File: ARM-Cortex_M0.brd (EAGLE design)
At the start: 50 x 50 mm, 26 parts, among them IC1 SAMD21G18A-AUT, J2 CORTEX_DEBUGPTH, U1 MIC5203-3.3, X1 MINI-USB_SHIELD4P-32005-101, Y3 32,768Khz_SMD

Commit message: hardware modifications
hardware modifications
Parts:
- removed J11: (no value), SparkFun-Connectors:USB-B-MICRO-SMD_V03
- removed X1: MINI-USB_SHIELD4P-32005-101, con-cypressindustries:32005-101
- added J13: USB-MICROB", KarlVaello-Connectors:USB-B-MICRO-SMD_V03
- moved C8 5.00 mm to (16.4, 12.6)
- moved R1 1.14 mm to (19.1, 12.6)
- moved R2 0.30 mm to (19.1, 16.6)
- moved C4 0.30 mm to (24.3, 16.6)
- moved C5 0.22 mm to (21.7, 16.6)
- moved C6 0.10 mm to (24.8, 33.1)
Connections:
- net GND: now also J13.GND, J13.SHIELD1, J13.SHIELD2, J13.SHIELD3; no longer J11.GND, J11.SHIELD1, J11.SHIELD2, J11.SHIELD3
- net TARGET_USB_N: now also J13.D-; no longer J11.D-
- net TARGET_USB_P: now also J13.D+; no longer J11.D+
- net VBUS: now also J13.VBUS; no longer J11.VBUS
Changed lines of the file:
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@@
 <layer number="23" name="tOrigins" color="15" fill="1" visible="yes" active="yes"/>
 <layer number="24" name="bOrigins" color="15" fill="1" visible="yes" active="yes"/>
-<layer number="25" name="tNames" color="7" fill="1" visible="yes" active="yes"/>
-<layer number="26" name="bNames" color="7" fill="1" visible="yes" active="yes"/>
-<layer number="27" name="tValues" color="7" fill="1" visible="yes" active="yes"/>
-<layer number="28" name="bValues" color="7" fill="1" visible="yes" active="yes"/>
+<layer number="25" name="tNames" color="7" fill="1" visible="no" active="yes"/>
+<layer number="26" name="bNames" color="7" fill="1" visible="no" active="yes"/>
+<layer number="27" name="tValues" color="7" fill="1" visible="no" active="yes"/>
+<layer number="28" name="bValues" color="7" fill="1" visible="no" active="yes"/>
 <layer number="29" name="tStop" color="7" fill="3" visible="no" active="yes"/>
 <layer number="30" name="bStop" color="7" fill="6" visible="no" active="yes"/>
@@
 <element name="C2" library="KarlVaello-Capacitors" package="C0603" value="22pF" x="14" y="29.5" rot="R90"/>
 <element name="C3" library="KarlVaello-Capacitors" package="C0603" value="100nF" x="33.1" y="28.6" rot="R180"/>
-<element name="C4" library="KarlVaello-Capacitors" package="C0603" value="" x="24.3" y="16.9" rot="R270"/>
-<element name="C5" library="KarlVaello-Capacitors" package="C0603" value="100nF" x="21.5" y="16.5" rot="R90"/>
+<element name="C4" library="KarlVaello-Capacitors" package="C0603" value="" x="24.3" y="16.6" rot="R270"/>
+<element name="C5" library="KarlVaello-Capacitors" package="C0603" value="100nF" x="21.7" y="16.6" rot="R90"/>
 <element name="J2" library="SparkFun-Connectors" package="2X5-PTH-1.27MM" value="CORTEX_DEBUGPTH" x="8.5" y="27.1" rot="R90"/>
-<element name="C6" library="KarlVaello-Capacitors" package="C0603" value="1uF" x="24.7" y="33.1" rot="R270"/>
+<element name="C6" library="KarlVaello-Capacitors" package="C0603" value="1uF" x="24.8" y="33.1" rot="R270"/>
 <element name="U1" library="SparkFun-PowerIC" package="SOT23-5" value="MIC5203-3.3" x="12.9" y="17">
 <attribute name="PROD_ID" value="VREG-00822" x="12.9" y="17" size="1.778" layer="27" display="off"/>
@@
 <element name="J9" library="SparkFun-Connectors" package="1X01NS-KIT" value="" x="2.9" y="6.1"/>
 <element name="J10" library="SparkFun-Connectors" package="1X01NS-KIT" value="" x="2.9" y="4"/>
-<element name="J11" library="SparkFun-Connectors" package="USB-B-MICRO-SMD_V03" value="" x="48" y="25" rot="R180">
-<attribute name="PROD_ID" value="CONN-11752" x="48" y="25" size="1.778" layer="27" rot="R180" display="off"/>
-</element>
-<element name="X1" library="con-cypressindustries" package="32005-101" value="MINI-USB_SHIELD4P-32005-101" x="46.5" y="13.9" rot="R180">
-<attribute name="OC_NEWARK" value="unknown" x="46.5" y="13.9" size="1.778" layer="27" rot="R180" display="off"/>
-<attribute name="OC_FARNELL" value="unknown" x="46.5" y="13.9" size="1.778" layer="27" rot="R180" display="off"/>
-<attribute name="MPN" value="" x="46.5" y="13.9" size="1.778" layer="27" rot="R180" display="off"/>
-<attribute name="MF" value="" x="46.5" y="13.9" size="1.778" layer="27" rot="R180" display="off"/>
-</element>
 <element name="S1" library="SparkFun-Electromechanical" package="TACTILE-SWITCH-SMD" value="SW-MOME" x="42.8" y="4.1">
 <attribute name="PROD_ID" value="SWCH-08247" x="42.8" y="4.1" size="1.778" layer="27" display="off"/>
 </element>
-<element name="C8" library="KarlVaello-Capacitors" package="C0603" value="10nF" x="21.3" y="11.6" rot="R270"/>
-<element name="R1" library="KarlVaello-Resistors" package="R0603" value="330R" x="18.2" y="11.9" rot="R90"/>
-<element name="R2" library="KarlVaello-Resistors" package="R0603" value="10K" x="18.8" y="16.6" rot="R90"/>
+<element name="C8" library="KarlVaello-Capacitors" package="C0603" value="10nF" x="16.4" y="12.6" rot="R270"/>
+<element name="R1" library="KarlVaello-Resistors" package="R0603" value="330R" x="19.1" y="12.6" rot="R90"/>
+<element name="R2" library="KarlVaello-Resistors" package="R0603" value="10K" x="19.1" y="16.6" rot="R90"/>
+<element name="J13" library="KarlVaello-Connectors" package="USB-B-MICRO-SMD_V03" value="USB-MICROB&quot;" x="48" y="25" rot="R180">
+<attribute name="PROD_ID" value="CONN-11752" x="48" y="25" size="1.778" layer="27" rot="R180" display="off"/>
+</element>
 </elements>
 <signals>
@@
 </polygon>
 <via x="3" y="47" extent="1-16" drill="0.6" shape="square"/>
-<wire x1="20.725" y1="25.75" x2="19" y2="25.75" width="0.3" layer="1"/>
-<wire x1="19" y1="25.75" x2="19" y2="26" width="0.3" layer="1"/>
+<wire x1="20.725" y1="25.75" x2="19" y2="25.75" width="0.2" layer="1"/>
 <contactref element="IC1" pad="18"/>
 <contactref element="C3" pad="1"/>
 <contactref element="IC1" pad="35"/>
 <contactref element="C4" pad="2"/>
-<wire x1="29.275" y1="27.25" x2="27.5" y2="27.25" width="0.3" layer="1"/>
-<wire x1="27.5" y1="27.25" x2="27.5" y2="27" width="0.3" layer="1"/>
+<wire x1="29.275" y1="27.25" x2="27.5" y2="27.25" width="0.2" layer="1"/>
 <wire x1="24.75" y1="20.725" x2="24.75" y2="22.55" width="0.3" layer="1"/>
 <wire x1="24.75" y1="22.55" x2="24.8" y2="22.6" width="0.3" layer="1"/>
@@
 <contactref element="U1" pad="2"/>
 <contactref element="C7" pad="1"/>
-<contactref element="J11" pad="GND"/>
-<contactref element="J11" pad="SHIELD1"/>
-<contactref element="J11" pad="SHIELD3"/>
-<contactref element="J11" pad="SHIELD2"/>
 <contactref element="S1" pad="3"/>
 <contactref element="C8" pad="1"/>
-<wire x1="27.5" y1="27.25" x2="25.25" y2="29.275" width="0" layer="19" extent="1-1"/>
+<contactref element="J13" pad="GND"/>
+<contactref element="J13" pad="SHIELD2"/>
+<contactref element="J13" pad="SHIELD1"/>
+<contactref element="J13" pad="SHIELD3"/>
+<wire x1="25.25" y1="29.275" x2="25.2" y2="29.275" width="0.1524" layer="1"/>
+<wire x1="25.2" y1="29.275" x2="25.2" y2="30.2" width="0.1524" layer="1"/>
 </signal>
 <signal name="+3V3">
@@
 <wire x1="24.25" y1="29.275" x2="29.275" y2="27.75" width="0" layer="19" extent="1-1"/>
 <wire x1="24.25" y1="20.725" x2="24.25" y2="29.275" width="0" layer="19" extent="1-1"/>
-<wire x1="24.3" y1="17.75" x2="24.25" y2="20.725" width="0" layer="19" extent="1-1"/>
-<wire x1="21.5" y1="17.35" x2="24.3" y2="17.75" width="0" layer="19" extent="1-1"/>
-<wire x1="18.8" y1="17.45" x2="21.5" y2="17.35" width="0" layer="19" extent="1-1"/>
-<wire x1="11.95" y1="18.3001" x2="18.8" y2="17.45" width="0" layer="19" extent="1-1"/>
+<wire x1="24.3" y1="17.45" x2="24.25" y2="20.725" width="0" layer="19" extent="1-1"/>
+<wire x1="21.7" y1="17.45" x2="24.3" y2="17.45" width="0" layer="19" extent="1-1"/>
+<wire x1="19.1" y1="17.45" x2="21.7" y2="17.45" width="0" layer="19" extent="1-1"/>
+<wire x1="11.95" y1="18.3001" x2="19.1" y2="17.45" width="0" layer="19" extent="1-1"/>
 <wire x1="9.15" y1="22.5" x2="11.95" y2="18.3001" width="0" layer="19" extent="1-1"/>
 <wire x1="9.135" y1="24.56" x2="9.15" y2="22.5" width="0" layer="19" extent="1-1"/>
@@
 <contactref element="R2" pad="1"/>
 <contactref element="S1" pad="1"/>
-<wire x1="18.2" y1="12.75" x2="40.006" y2="6.005" width="0" layer="19" extent="1-1"/>
-<wire x1="18.8" y1="15.75" x2="18.2" y2="12.75" width="0" layer="19" extent="1-1"/>
-<wire x1="7.865" y1="29.64" x2="18.8" y2="15.75" width="0" layer="19" extent="1-1"/>
+<wire x1="19.1" y1="13.45" x2="40.006" y2="6.005" width="0" layer="19" extent="1-1"/>
+<wire x1="19.1" y1="15.75" x2="19.1" y2="13.45" width="0" layer="19" extent="1-1"/>
+<wire x1="7.865" y1="29.64" x2="19.1" y2="15.75" width="0" layer="19" extent="1-1"/>
 </signal>
 <signal name="N$7">
 <contactref element="IC1" pad="43"/>
 <contactref element="C6" pad="2"/>
-<wire x1="24.75" y1="29.275" x2="24.7" y2="32.25" width="0" layer="19" extent="1-1"/>
+<wire x1="24.75" y1="29.275" x2="24.8" y2="32.25" width="0" layer="19" extent="1-1"/>
 </signal>
 <signal name="RAW">
@@
 <wire x1="11.95" y1="15.6999" x2="13.85" y2="15.6999" width="0" layer="19" extent="1-1"/>
 </signal>
-<signal name="VBUS">
-<contactref element="J11" pad="VBUS"/>
-</signal>
 <signal name="TARGET_USB_N">
-<contactref element="J11" pad="D-"/>
 <contactref element="IC1" pad="33"/>
 <wire x1="29.275" y1="26.25" x2="40.25" y2="26.25" width="0.1524" layer="1"/>
 <wire x1="40.25" y1="26.25" x2="42.15" y2="24.35" width="0.1524" layer="1"/>
+<contactref element="J13" pad="D-"/>
 <wire x1="42.15" y1="24.35" x2="45.275" y2="24.35" width="0.1524" layer="1"/>
 </signal>
 <signal name="TARGET_USB_P">
-<contactref element="J11" pad="D+"/>
 <contactref element="IC1" pad="34"/>
 <wire x1="29.275" y1="26.75" x2="40.55" y2="26.75" width="0.1524" layer="1"/>
 <wire x1="40.55" y1="26.75" x2="42.3" y2="25" width="0.1524" layer="1"/>
+<contactref element="J13" pad="D+"/>
 <wire x1="42.3" y1="25" x2="45.275" y2="25" width="0.1524" layer="1"/>
 </signal>
@@
 <contactref element="C8" pad="2"/>
 <contactref element="R1" pad="1"/>
-<wire x1="21.3" y1="10.75" x2="26.25" y2="29.275" width="0" layer="19" extent="1-1"/>
-<wire x1="18.2" y1="11.05" x2="21.3" y2="10.75" width="0" layer="19" extent="1-1"/>
+<wire x1="19.1" y1="11.75" x2="26.25" y2="29.275" width="0" layer="19" extent="1-1"/>
+<wire x1="16.4" y1="11.75" x2="19.1" y2="11.75" width="0" layer="19" extent="1-1"/>
 </signal>
 <signal name="D13">
@@
 <contactref element="IC1" pad="16"/>
 </signal>
+<signal name="VBUS">
+<contactref element="J13" pad="VBUS"/>
+</signal>
 </signals>

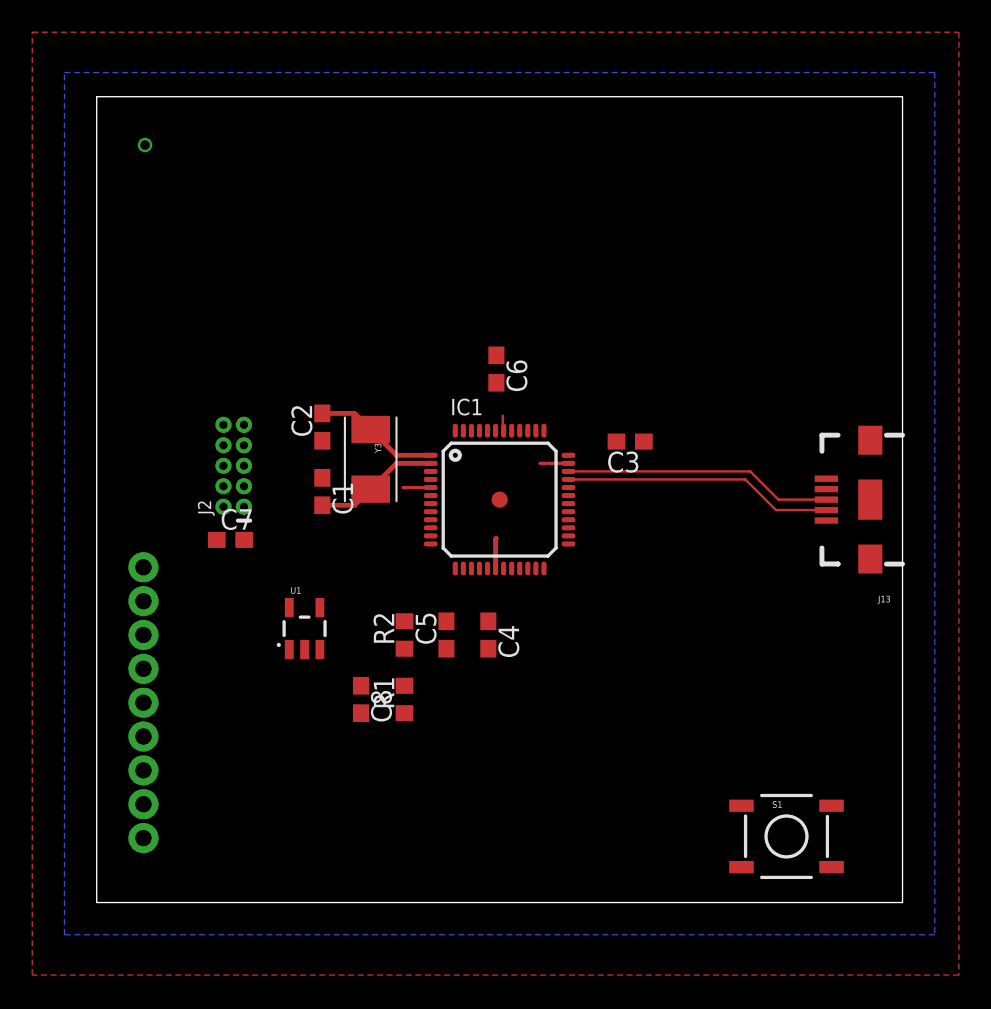
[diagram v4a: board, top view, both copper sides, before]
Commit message: Hardaware modification, programing ARM info
Hardaware modification, programing ARM info
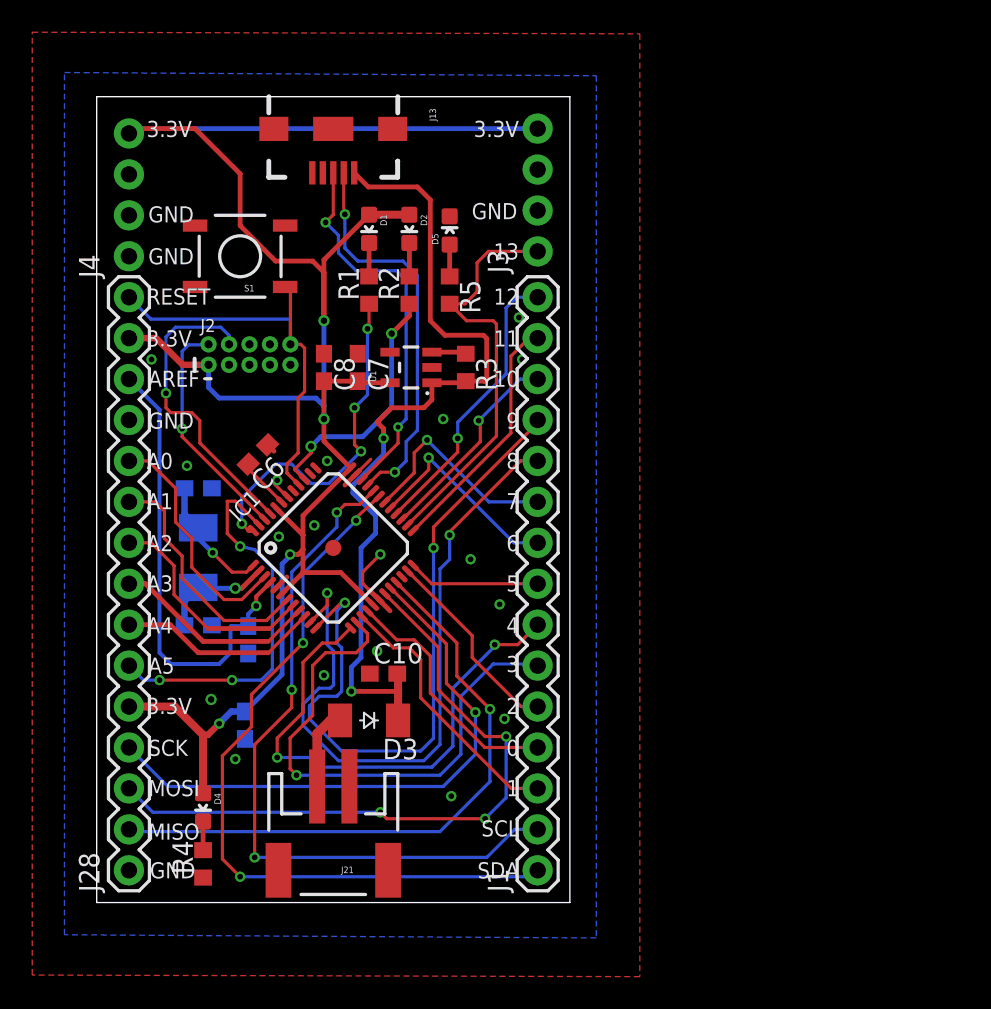
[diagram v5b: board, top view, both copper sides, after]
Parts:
- removed C3: 100nF, KarlVaello-Capacitors:C0603
- removed C4: (no value), KarlVaello-Capacitors:C0603
- removed J10, J5, J6, J7, J8, J9: (no value), SparkFun-Connectors:1X01NS-KIT
- added C10: 10uF, KarlVaello-Capacitors:C0603
- added C9: 1uF, KarlVaello-Capacitors:C0603
- added D1, D5: GREEN, SparkFun-LED:LED-0603
- added D2: YELLOW, SparkFun-LED:LED-0603
- added D3: MBR120, diode:SOD-123_MINI-SMA
- added D4: ORANGE, SparkFun-LED:LED-0603
- added J21: (no value), SparkFun-Connectors:JST-2-SMD
- added J28: (no value), SparkFun-Connectors:1X15
- added R3: 100K, KarlVaello-Resistors:R0603
- added R4, R5: 1K, KarlVaello-Resistors:R0603
- C5: value 100nF -> 10uF
- C8: value 10nF -> 10uF
- J1: device SparkFun-Connectors:1X01NS-KIT -> SparkFun-Connectors:1X15
- J3, J4: device SparkFun-Connectors:1X01NS-KIT -> SparkFun-Connectors:1X04_NO_SILK_ALL_ROUND
- R1: value 330R -> 1K
- R2: value 10K -> 1K
- U1: value MIC5203-3.3 -> SPX3918-3.3
- moved S1 49.4 mm to (8.90, 40.1), turned to 180 degrees
- moved J13 40.5 mm to (14.7, 48.0), turned to 270 degrees
- moved J3 32.7 mm to (27.4, 40.4), turned to 90 degrees
- moved J1 30.9 mm to (27.4, 2.00), turned to 90 degrees
- moved R1 25.5 mm to (16.9, 38.0)
- moved J4 23.5 mm to (2.00, 40.1), turned to 90 degrees
- moved R2 21.4 mm to (19.4, 38.0)
- moved C8 20.7 mm to (14.1, 33.2)
- moved U1 17.5 mm to (19.5, 33.2), turned to 90 degrees
- moved C6 15.7 mm to (10.0, 27.8), turned to 225 degrees
- moved C5 13.7 mm to (9.20, 11.0), flipped to the bottom
- moved C7 13.3 mm to (16.2, 33.2), turned to 270 degrees
- moved Y3 12.3 mm to (6.30, 21.4), flipped to the bottom
- moved C1 11.3 mm to (6.30, 17.2), flipped to the bottom, turned to 0 degrees
- moved IC1 10.7 mm to (14.7, 22.0), turned to 45 degrees
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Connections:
- removed net D0: IC1.16
- removed net D1: IC1.15
- removed net RAW: U1.1, U1.3
- removed net TARGE_RESET: C8.2, IC1.40, R1.1
- removed net VDDANA: IC1.6
- new net A0: IC1.3, J28.11
- new net A1: IC1.7, J28.10
- new net A2: IC1.8, J28.9
- new net A3: IC1.9, J28.8
- new net A4: IC1.10, J28.7
- new net A5: IC1.47, J28.6
- new net AREF: C9.2, IC1.4, J28.13
- new net D0/RX: IC1.16, J1.4
- new net D1/TX: IC1.15, J1.3
- new net MISO: IC1.21, J28.2
- new net MOSI: IC1.19, J28.3
- new net N$10: D5.A, R5.1
- new net N$3: IC1.22
- new net N$4: D1.C, R1.2
- new net N$5: D2.C, R2.2
- new net N$6: R3.1, U1.3
- new net N$8: D4.C, R4.2
- new net RDX: IC1.38
- new net RX_LED: IC1.48, R1.1
- new net SCK: IC1.20, J28.4
- new net SCL: IC1.32, J1.2
- new net SDA: IC1.31, J1.1
- new net TDX: IC1.37
- new net TX_LED: IC1.39, R2.1
- new net USBHOSTEN: IC1.41
- new net VBAT: D3.A, J21.2
- net +3V3: now also C8.2, D1.A, D2.A, D4.A, IC1.6, J28.14, J28.5, J3.4, J4.4; no longer C3.2, C4.1, R2.2
- net D10: now also J1.13
- net D11: now also J1.14
- net D12: now also J1.15
- net D13: now also J3.1, R5.2
- net D2: now also J1.5
- net D3: now also J1.6
- net D4: now also J1.7
- net D5: now also J1.8
- net D6: now also J1.9
- net D7: now also J1.10
- net D8: now also J1.11
- net D9: now also J1.12
- net GND: now also C10.1, C9.1, D5.C, J21.1, J28.1, J28.12, J3.2, J4.1, J4.2, R4.1; no longer C3.1, C4.2
- net RESET: now also IC1.40, J28.15; no longer R1.2, R2.1
- net VBUS: now also C10.2, D3.C, R3.2, U1.1
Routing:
- net +3V3: track 0.00 -> 128.7 mm, vias 0 -> 4
- net VBUS: track 0.00 -> 54.7 mm, vias 0 -> 2
- net SDA: track 0.00 -> 46.7 mm, vias 0 -> 3
- net SCL: track 0.00 -> 44.6 mm, vias 0 -> 3
- net D9: track 0.00 -> 42.7 mm, vias 0 -> 2
- net D8: track 0.00 -> 42.5 mm, vias 0 -> 2
- net MOSI: track 0.00 -> 41.2 mm, vias 0 -> 3
- net MISO: track 0.00 -> 38.5 mm, vias 0 -> 1
- net SCK: track 0.00 -> 35.8 mm, vias 0 -> 1
- net D3: track 0.00 -> 33.0 mm, vias 0 -> 1
- net D4: track 0.00 -> 32.6 mm, vias 0 -> 2
- net AREF: track 0.00 -> 28.7 mm, vias 0 -> 1
- net RESET: track 0.00 -> 26.1 mm
- net D13: track 0.00 -> 26.0 mm
- net A5: track 0.00 -> 24.0 mm, vias 0 -> 3
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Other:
- board size 50 x 50 mm -> 29.4 x 50 mm
- board text added: "0"
- board text added: "1"
- board text added: "10"
- board text added: "11"
- board text added: "12"
- board text added: "13"
- board text added: "2"
- board text added: "3"
- board text added: "3.3V"
- board text added: "4"
- board text added: "5"
- board text added: "6"
- board text added: "7"
- board text added: "8"
- board text added: "9"
- board text added: "A0"
- board text added: "A1"
- board text added: "A2"
- board text added: "A3"
- board text added: "A4"
- board text added: "A5"
- board text added: "AREF"
- board text added: "GND"
- board text added: "MISO"
- board text added: "MOSI"
- board text added: "RESET"
- board text added: "SCK"
- board text added: "SCL"
- board text added: "SDA"
